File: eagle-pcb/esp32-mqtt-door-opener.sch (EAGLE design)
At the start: 14 parts, among them IC1 LM1117MP-3.3, K1 S202S02, U1 ESP-WROOM-32

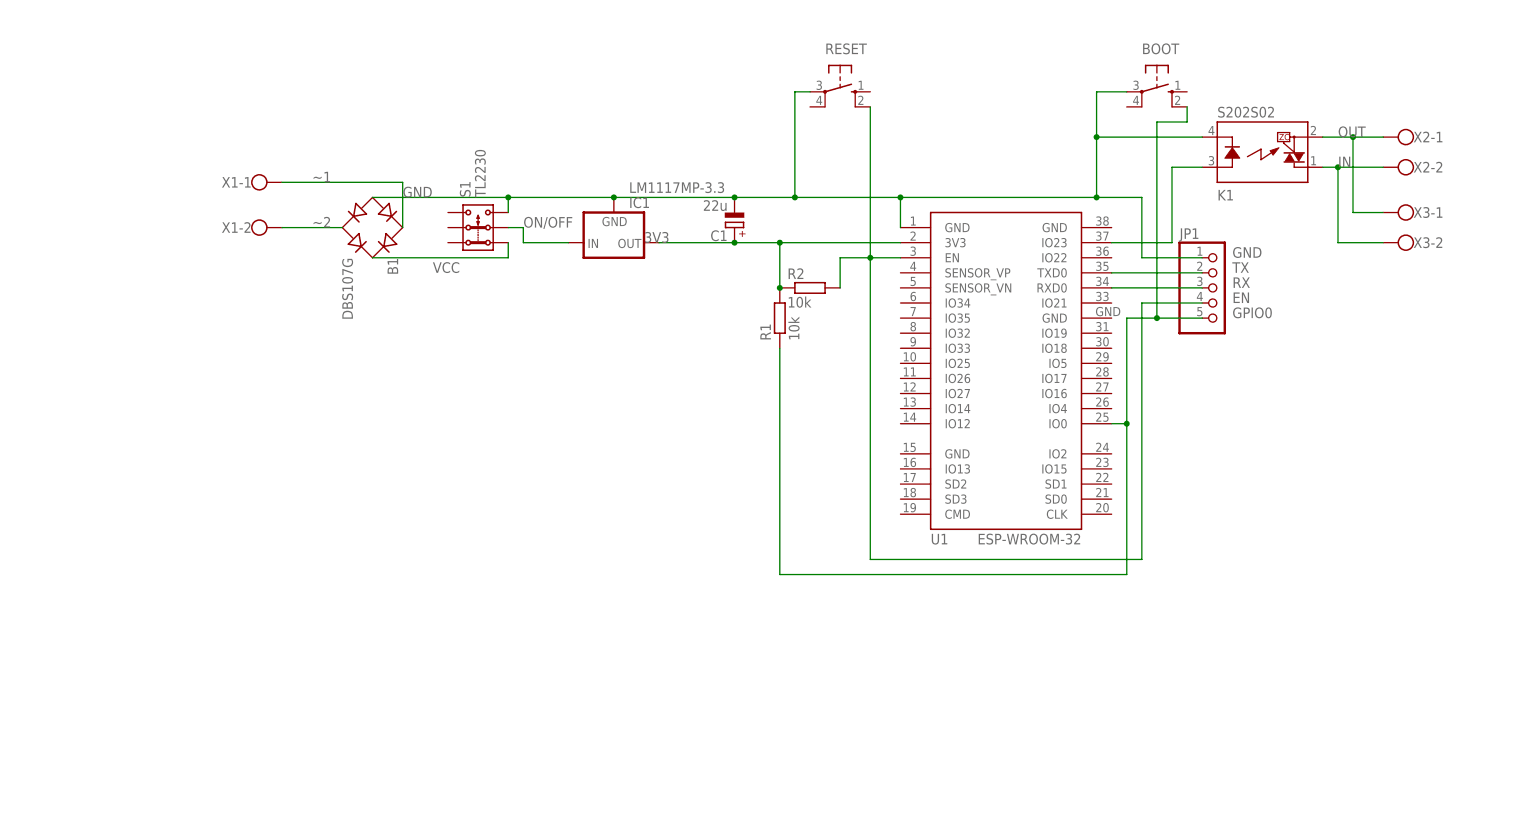
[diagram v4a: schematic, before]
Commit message: pcb: revise schematic to 4.0
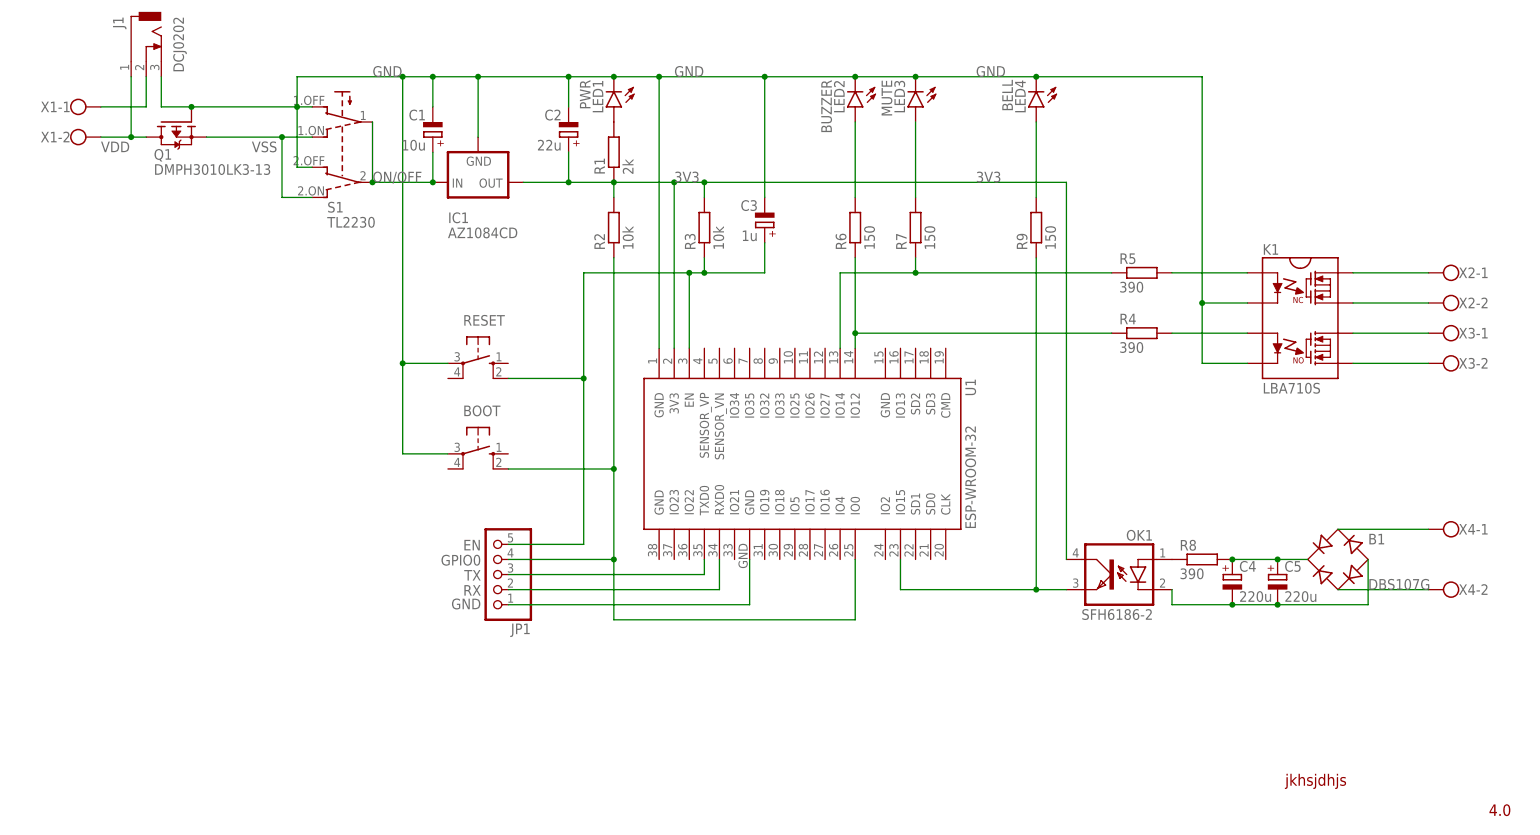
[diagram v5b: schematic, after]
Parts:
- added C2: 22u, rcl:CPOL-EUC/6032-28R
- added C3: 1u, rcl:CPOL-EUA/3216-18R
- added C4, C5: 220u, rcl:CPOL-EUD/7343-31R
- added J1: DCJ0202, con-jack:DCJ0202
- added LED1: PWR, led:LEDSMT1206
- added LED2: BUZZER, led:LEDSMT1206
- added LED3: MUTE, led:LEDSMT1206
- added LED4: BELL, led:LEDSMT1206
- added OK1: SFH6186-2, optocoupler:SFH6186-2
- added Q1: DMPH3010LK3-13, transistor-fet:FDD4141TO252
- added R3: 10k, rcl:R-EU_R0603
- added R4, R5, R8: 390, rcl:R-EU_R0603
- added R6, R7, R9: 150, rcl:R-EU_R0603
- added X4: (no value), con-wago-500:W237-102
- C1: value 22u -> 10u; device rcl:CPOL-EUSMCC -> rcl:CPOL-EUC/6032-28R
- IC1: value LM1117MP-3.3 -> AZ1084CD; device lm1117_10:LM1117MP-3.3 -> AZ1084C:AZ1084CD
- K1: value S202S02 -> LBA710S; device S202S02:S202S02 -> LBA710:LBA710S
- R1: value 10k -> 2k; device rcl:R-EU_R1206 -> rcl:R-EU_R0603
- R2: device rcl:R-EU_R1206 -> rcl:R-EU_R0603
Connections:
- removed net GPIO23: K1.A, U1.IO23
- removed net IN: K1.DS1, X2-2.KL, X3-2.KL
- removed net OUT: K1.DS2, X2-1.KL, X3-1.KL
- removed net VCC: B1.+, S1.1.2
- removed net ~1: B1.AC1, X1-1.KL
- removed net ~2: B1.AC2, X1-2.KL
- new net N$1: LED1.A, R1.2
- new net N$10: K1.NC-OUT2, X2-2.KL
- new net N$11: K1.NO-OUT1, X3-1.KL
- new net N$12: K1.NO-OUT2, X3-2.KL
- new net N$13: B1.AC2, X4-2.KL
- new net N$14: R5.1, R7.1, U1.IO14
- new net N$15: B1.+, C4.+, C5.+, R8.2
- new net N$16: B1.-, C4.-, C5.-, OK1.C
- new net N$17: OK1.A, R8.1
- new net N$18: LED4.A, R9.2
- new net N$2: OK1.EMIT, R9.1, U1.IO15
- new net N$20: J1.2, X1-1.KL
- new net N$3: K1.NO-CONTROL+, R4.2
- new net N$4: LED3.A, R7.2
- new net N$5: K1.NC-CONTROL+, R5.2
- new net N$6: LED2.A, R6.2
- new net N$7: R4.1, R6.1, U1.IO12
- new net N$8: B1.AC1, X4-1.KL
- new net N$9: K1.NC-OUT1, X2-1.KL
- new net VDD: J1.1, Q1.D, X1-2.KL
- new net VSS: Q1.S, S1.1.ON, S1.2.ON
- net 3V3: now also C2.+, OK1.COL, R1.1, R2.2, R3.2; no longer C1.+, R1.2, R2.1
- net EN: now also C3.+, JP1.5, R3.1; no longer JP1.4, R2.2
- net GND: now also C2.-, C3.-, J1.3, K1.NC-CONTROL-, K1.NO-CONTROL-, LED1.C, LED2.C, LED3.C, LED4.C, Q1.G, S1.1.OFF, S1.2.OFF, U1.GND@4; no longer B1.-, K1.K, S1.3.2
- net GPIO0: now also JP1.4, R2.1; no longer JP1.5, R1.1
- net ON/OFF: now also C1.+, S1.1, S1.2; no longer S1.2.2
- net RX: now also JP1.2; no longer JP1.3
- net TX: now also JP1.3; no longer JP1.2
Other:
- moved on the sheet: B1, BOOT, C1, IC1, JP1, R1, R2, RESET, U1, X1-1, X1-2, X2-1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

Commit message: pcb: use 330 ohm resistors instead of 390 + use ESP32-WROOM-32D
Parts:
- R4, R5, R8: value 390 -> 330
- U1: value ESP-WROOM-32 -> ESP-WROOM-32D
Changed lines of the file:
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@@
 <part name="JP1" library="pinhead" library_urn="urn:adsk.eagle:library:325" deviceset="PINHD-1X5" device="" package3d_urn="urn:adsk.eagle:package:22469/2"/>
 <part name="X1" library="con-wago-500" library_urn="urn:adsk.eagle:library:195" deviceset="W237-102" device="" package3d_urn="urn:adsk.eagle:package:10688/1"/>
-<part name="U1" library="esp32" deviceset="ESP-WROOM-32" device=""/>
+<part name="U1" library="esp32" deviceset="ESP-WROOM-32" device="" value="ESP-WROOM-32D"/>
 <part name="X2" library="con-wago-500" library_urn="urn:adsk.eagle:library:195" deviceset="W237-102" device="" package3d_urn="urn:adsk.eagle:package:10688/1"/>
 <part name="X3" library="con-wago-500" library_urn="urn:adsk.eagle:library:195" deviceset="W237-102" device="" package3d_urn="urn:adsk.eagle:package:10688/1"/>
@@
 <part name="K1" library="LBA710" deviceset="LBA710" device="S"/>
 <part name="OK1" library="optocoupler" library_urn="urn:adsk.eagle:library:320" deviceset="SFH618?*" device="6" package3d_urn="urn:adsk.eagle:package:21961/1" technology="-2"/>
-<part name="R4" library="rcl" library_urn="urn:adsk.eagle:library:334" deviceset="R-EU_" device="R0603" package3d_urn="urn:adsk.eagle:package:23555/3" value="390"/>
-<part name="R5" library="rcl" library_urn="urn:adsk.eagle:library:334" deviceset="R-EU_" device="R0603" package3d_urn="urn:adsk.eagle:package:23555/3" value="390"/>
+<part name="R4" library="rcl" library_urn="urn:adsk.eagle:library:334" deviceset="R-EU_" device="R0603" package3d_urn="urn:adsk.eagle:package:23555/3" value="330"/>
+<part name="R5" library="rcl" library_urn="urn:adsk.eagle:library:334" deviceset="R-EU_" device="R0603" package3d_urn="urn:adsk.eagle:package:23555/3" value="330"/>
 <part name="R7" library="rcl" library_urn="urn:adsk.eagle:library:334" deviceset="R-EU_" device="R0603" package3d_urn="urn:adsk.eagle:package:23555/3" value="150"/>
 <part name="R6" library="rcl" library_urn="urn:adsk.eagle:library:334" deviceset="R-EU_" device="R0603" package3d_urn="urn:adsk.eagle:package:23555/3" value="150"/>
@@
 <part name="LED3" library="led" library_urn="urn:adsk.eagle:library:259" deviceset="LED" device="SMT1206" package3d_urn="urn:adsk.eagle:package:15796/2" value="MUTE"/>
 <part name="LED2" library="led" library_urn="urn:adsk.eagle:library:259" deviceset="LED" device="SMT1206" package3d_urn="urn:adsk.eagle:package:15796/2" value="BUZZER"/>
-<part name="R8" library="rcl" library_urn="urn:adsk.eagle:library:334" deviceset="R-EU_" device="R0603" package3d_urn="urn:adsk.eagle:package:23555/3" value="390"/>
+<part name="R8" library="rcl" library_urn="urn:adsk.eagle:library:334" deviceset="R-EU_" device="R0603" package3d_urn="urn:adsk.eagle:package:23555/3" value="330"/>
 <part name="R9" library="rcl" library_urn="urn:adsk.eagle:library:334" deviceset="R-EU_" device="R0603" package3d_urn="urn:adsk.eagle:package:23555/3" value="150"/>
 <part name="LED4" library="led" library_urn="urn:adsk.eagle:library:259" deviceset="LED" device="SMT1206" package3d_urn="urn:adsk.eagle:package:15796/2" value="BELL"/>

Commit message: pcb: adjust some labels
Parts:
- removed X2, X3, X4: (no value), con-wago-500:W237-102
- added BELL, BUZZER, MUTE: (no value), con-wago-500:W237-102
- renumbered X1 to PWR
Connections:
- net N$14 renamed GPIO14
- net N$2 renamed GPIO15
- net N$7 renamed GPIO12
- net N$10: now also MUTE-2.KL; no longer X2-2.KL
- net N$11: now also BUZZER-1.KL; no longer X3-1.KL
- net N$12: now also BUZZER-2.KL; no longer X3-2.KL
- net N$13: now also BELL-2.KL; no longer X4-2.KL
- net N$8: now also BELL-1.KL; no longer X4-1.KL
- net N$9: now also MUTE-1.KL; no longer X2-1.KL
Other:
- moved on the sheet: B1, BOOT, C1, C2, C3, C4, C5, IC1, J1, JP1, K1, LED1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
